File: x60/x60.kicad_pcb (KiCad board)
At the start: 2 copper layers, 0.1 x 0.5 mm, 150 parts, among them SW1 SW_Push, U1 ATmega32U4-AU, Y1 16mhz

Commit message: rearranged lines after stabs flip
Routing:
- net COL3: track 242.7 -> 248.7 mm
- net COL5: track 176.8 -> 177.8 mm
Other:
- board size 0.1 x 0.5 mm -> 285.7 x 95.2 mm
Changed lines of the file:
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@@
   (general
     (thickness 1.6)
-    (drawings 4)
-    (tracks 1052)
+    (drawings 5)
+    (tracks 1055)
     (zones 0)
     (modules 150)
@@
     )
   )
-  (gr_line (start 69.265 112.985) (end 69.325 112.715) (layer Edge.Cuts) (width 0.05))
-  (gr_line (start 69.245 113.035) (end 69.265 112.985) (layer Edge.Cuts) (width 0.05))
-  (gr_line (start 69.235 113.205) (end 69.245 113.035) (layer Edge.Cuts) (width 0.05))
+  (gr_line (start 69.325 204.405) (end 355.025 204.425) (layer Edge.Cuts) (width 0.05))
+  (gr_line (start 69.325 109.205) (end 69.325 204.405) (layer Edge.Cuts) (width 0.05))
+  (gr_line (start 355.025 109.225) (end 69.325 109.205) (layer Edge.Cuts) (width 0.05))
+  (gr_line (start 355.025 204.425) (end 355.025 109.225) (layer Edge.Cuts) (width 0.05))
   (gr_text x60 (at 311.29375 276.78125) (layer F.Cu)
     (effects (font (size 1.5 1.5) (thickness 0.3)))
@@
   (segment (start 72.5325 121.64625) (end 88.17875 121.64625) (width 0.254) (layer B.Cu) (net 7))
   (segment (start 71.4275 122.75125) (end 72.5325 121.64625) (width 0.254) (layer B.Cu) (net 7))
-  (segment (start 71.4275 142.739183) (end 71.4275 122.75125) (width 0.254) (layer B.Cu) (net 7))
   (segment (start 71.34948 142.817203) (end 71.4275 142.739183) (width 0.254) (layer B.Cu) (net 7))
-  (segment (start 182.46875 199.49525) (end 178.46496 203.49904) (width 0.254) (layer B.Cu) (net 7))
-  (segment (start 182.46875 198.49125) (end 182.46875 199.49525) (width 0.254) (layer B.Cu) (net 7))
-  (segment (start 178.46496 203.49904) (end 167.93529 203.49904) (width 0.254) (layer B.Cu) (net 7))
-  (segment (start 167.93529 203.49904) (end 164.243577 199.807327) (width 0.254) (layer B.Cu) (net 7))
   (segment (start 71.34948 198.335297) (end 71.34948 142.817203) (width 0.254) (layer B.Cu) (net 7))
-  (segment (start 164.243577 199.807327) (end 72.82151 199.807327) (width 0.254) (layer B.Cu) (net 7))
+  (segment (start 182.46875 198.49125) (end 182.46875 199.49525) (width 0.254) (layer B.Cu) (net 7))
+  (segment (start 178.46496 203.49904) (end 167.941156 203.49904) (width 0.254) (layer B.Cu) (net 7))
+  (segment (start 182.46875 199.49525) (end 178.46496 203.49904) (width 0.254) (layer B.Cu) (net 7))
+  (segment (start 167.941156 203.49904) (end 167.675203 203.233086) (width 0.254) (layer B.Cu) (net 7))
+  (segment (start 167.675203 203.233086) (end 164.249444 199.807327) (width 0.254) (layer B.Cu) (net 7))
+  (segment (start 71.4275 142.739183) (end 71.4275 122.75125) (width 0.254) (layer B.Cu) (net 7))
   (segment (start 72.82151 199.807327) (end 71.34948 198.335297) (width 0.254) (layer B.Cu) (net 7))
+  (segment (start 164.249444 199.807327) (end 72.82151 199.807327) (width 0.254) (layer B.Cu) (net 7))
   (segment (start 86.10625 132.67875) (end 94.7425 132.67875) (width 0.254) (layer B.Cu) (net 8))
   (segment (start 94.7425 132.67875) (end 95.61625 133.5525) (width 0.254) (layer B.Cu) (net 8))
@@
   (segment (start 186.376392 202.93076) (end 184.052191 200.606559) (width 0.254) (layer B.Cu) (net 15))
   (segment (start 139.12875 197.19625) (end 139.1625 197.19625) (width 0.254) (layer B.Cu) (net 15))
-  (segment (start 139.1625 197.19625) (end 139.7875 197.82125) (width 0.254) (layer B.Cu) (net 15))
   (via (at 164.563963 197.57326) (size 0.8) (drill 0.4) (layers F.Cu B.Cu) (net 15))
-  (segment (start 139.7875 197.82125) (end 140.03549 197.57326) (width 0.254) (layer B.Cu) (net 15))
   (segment (start 140.03549 197.57326) (end 164.563963 197.57326) (width 0.254) (layer B.Cu) (net 15))
   (segment (start 168.57625 200.59) (end 184.06875 200.59) (width 0.254) (layer F.Cu) (net 15))
@@
   (segment (start 164.563963 197.57326) (end 165.55951 197.57326) (width 0.254) (layer F.Cu) (net 15))
   (via (at 184.06875 200.59) (size 0.8) (drill 0.4) (layers F.Cu B.Cu) (net 15))
+  (segment (start 139.12875 197.19625) (end 139.20625 197.19625) (width 0.254) (layer B.Cu) (net 15))
+  (segment (start 139.58326 197.57326) (end 140.03549 197.57326) (width 0.254) (layer B.Cu) (net 15))
+  (segment (start 139.20625 197.19625) (end 139.58326 197.57326) (width 0.254) (layer B.Cu) (net 15))
   (segment (start 100.39375 113.62875) (end 104.68 113.62875) (width 0.254) (layer B.Cu) (net 16))
   (segment (start 104.68 113.62875) (end 105.79125 114.74) (width 0.254) (layer B.Cu) (net 16))
@@
   (segment (start 130.509375 184.320625) (end 128.09625 186.73375) (width 0.254) (layer F.Cu) (net 75))
   (segment (start 101.1875 192.36875) (end 103.56875 192.36875) (width 0.254) (layer B.Cu) (net 75))
-  (segment (start 178.81095 203.95305) (end 167.6793 203.95305) (width 0.254) (layer B.Cu) (net 75))
-  (segment (start 183.26875 198.49125) (end 183.26875 199.49525) (width 0.254) (layer B.Cu) (net 75))
-  (segment (start 183.26875 199.49525) (end 178.81095 203.95305) (width 0.254) (layer B.Cu) (net 75))
-  (segment (start 167.6793 203.95305) (end 166.1575 202.43125) (width 0.254) (layer B.Cu) (net 75))
-  (via (at 101.2375 200.534327) (size 0.8) (drill 0.4) (layers F.Cu B.Cu) (net 75))
-  (segment (start 166.1575 202.43125) (end 164.260577 200.534327) (width 0.254) (layer B.Cu) (net 75))
-  (segment (start 164.260577 200.534327) (end 101.2375 200.534327) (width 0.254) (layer B.Cu) (net 75))
-  (segment (start 99.59651 192.36875) (end 101.1875 192.36875) (width 0.254) (layer F.Cu) (net 75))
-  (segment (start 98.715499 193.249761) (end 99.59651 192.36875) (width 0.254) (layer F.Cu) (net 75))
-  (segment (start 98.715499 197.446641) (end 98.715499 193.249761) (width 0.254) (layer F.Cu) (net 75))
-  (segment (start 101.2375 199.968642) (end 98.715499 197.446641) (width 0.254) (layer F.Cu) (net 75))
-  (segment (start 101.2375 200.534327) (end 101.2375 199.968642) (width 0.254) (layer F.Cu) (net 75))
+  (segment (start 99.59651 192.36875) (end 99.59026 192.375) (width 0.254) (layer F.Cu) (net 75))
+  (segment (start 101.1875 192.36875) (end 99.59651 192.36875) (width 0.254) (layer F.Cu) (net 75))
+  (segment (start 99.59026 192.375) (end 97.875 192.375) (width 0.254) (layer F.Cu) (net 75))
+  (segment (start 97.875 192.375) (end 97.025 193.225) (width 0.254) (layer F.Cu) (net 75))
+  (segment (start 97.025 193.225) (end 97.025 202.485) (width 0.254) (layer F.Cu) (net 75))
+  (via (at 99.645006 203.782122) (size 0.8) (drill 0.4) (layers F.Cu B.Cu) (net 75))
+  (segment (start 97.025 202.485) (end 98.322122 203.782122) (width 0.254) (layer F.Cu) (net 75))
+  (segment (start 98.322122 203.782122) (end 99.645006 203.782122) (width 0.254) (layer F.Cu) (net 75))
+  (segment (start 183.26875 199.49525) (end 183.26875 198.49125) (width 0.254) (layer B.Cu) (net 75))
+  (segment (start 178.81095 203.95305) (end 183.26875 199.49525) (width 0.254) (layer B.Cu) (net 75))
+  (segment (start 100.381619 203.95305) (end 178.81095 203.95305) (width 0.254) (layer B.Cu) (net 75))
+  (segment (start 100.210691 203.782122) (end 100.381619 203.95305) (width 0.254) (layer B.Cu) (net 75))
+  (segment (start 99.645006 203.782122) (end 100.210691 203.782122) (width 0.254) (layer B.Cu) (net 75))
   (segment (start 134.58875 135.21875) (end 141.66875 135.21875) (width 0.254) (layer F.Cu) (net 76))
   (segment (start 133.71625 134.34625) (end 134.58875 135.21875) (width 0.254) (layer F.Cu) (net 76))
@@
   (segment (start 169.45 167.7625) (end 175.00625 173.31875) (width 0.254) (layer F.Cu) (net 100))
   (segment (start 162.37 167.7625) (end 169.45 167.7625) (width 0.254) (layer F.Cu) (net 100))
-  (segment (start 169.45 167.7625) (end 169.45 179.575) (width 0.254) (layer F.Cu) (net 100))
-  (segment (start 169.45 179.575) (end 163.085 185.94) (width 0.254) (layer F.Cu) (net 100))
-  (segment (start 163.085 185.94) (end 132.9225 185.94) (width 0.254) (layer F.Cu) (net 100))
-  (segment (start 128.506249 191.243751) (end 127.38125 192.36875) (width 0.254) (layer F.Cu) (net 100))
-  (segment (start 128.506249 190.356251) (end 128.506249 191.243751) (width 0.254) (layer F.Cu) (net 100))
-  (segment (start 132.9225 185.94) (end 128.506249 190.356251) (width 0.254) (layer F.Cu) (net 100))
   (segment (start 127.38125 192.36875) (end 125 192.36875) (width 0.254) (layer F.Cu) (net 100))
   (via (at 189.501468 180.807282) (size 0.8) (drill 0.4) (layers F.Cu B.Cu) (net 100))
@@
   (segment (start 188.33 173.31875) (end 175.00625 173.31875) (width 0.254) (layer F.Cu) (net 100))
   (segment (start 188.3775 173.27125) (end 188.33 173.31875) (width 0.254) (layer F.Cu) (net 100))
+  (segment (start 169.45 179.575) (end 169.45 167.7625) (width 0.254) (layer F.Cu) (net 100))
+  (segment (start 165.05 183.975) (end 169.45 179.575) (width 0.254) (layer F.Cu) (net 100))
+  (segment (start 133.265 183.975) (end 165.05 183.975) (width 0.254) (layer F.Cu) (net 100))
+  (segment (start 128.506249 188.733751) (end 133.265 183.975) (width 0.254) (layer F.Cu) (net 100))
+  (segment (start 127.38125 192.36875) (end 128.506249 191.243751) (width 0.254) (layer F.Cu) (net 100))
+  (segment (start 128.506249 191.243751) (end 128.506249 188.733751) (width 0.254) (layer F.Cu) (net 100))
 )

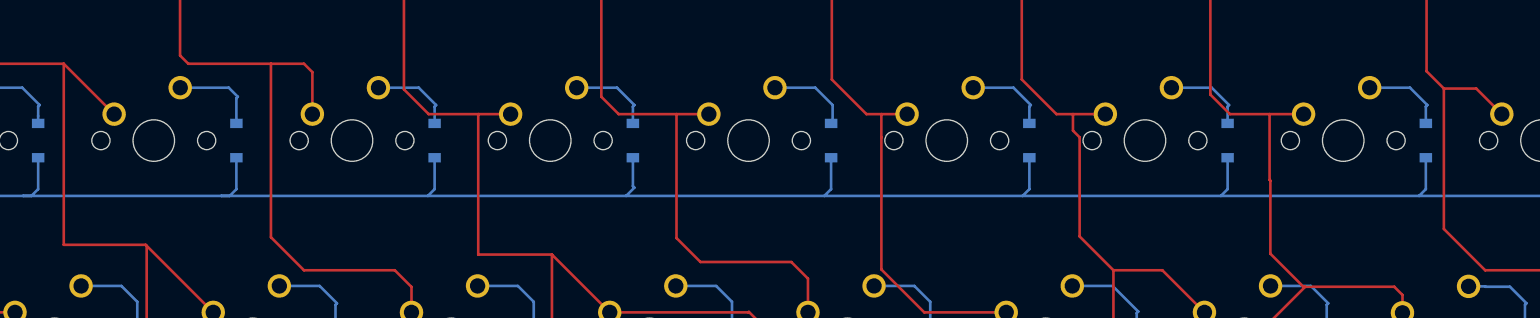
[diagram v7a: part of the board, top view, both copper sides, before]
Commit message: adjusted some routing
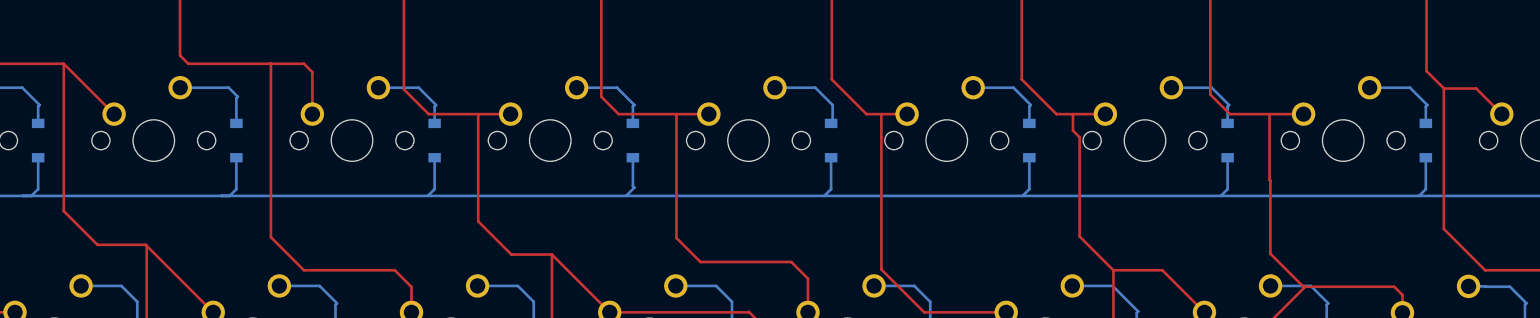
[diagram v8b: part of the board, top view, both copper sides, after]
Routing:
- net COL3: track 248.7 -> 246.8 mm
- net COL5: track 177.8 -> 175.9 mm
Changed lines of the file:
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@@
     (thickness 1.6)
     (drawings 5)
-    (tracks 1055)
+    (tracks 1058)
     (zones 0)
     (modules 150)
@@
   (segment (start 122.54 149.4275) (end 127.38125 154.26875) (width 0.254) (layer F.Cu) (net 75))
   (segment (start 114.66625 149.4275) (end 122.54 149.4275) (width 0.254) (layer F.Cu) (net 75))
-  (segment (start 122.54 149.4275) (end 122.54 166.82625) (width 0.254) (layer F.Cu) (net 75))
-  (segment (start 122.54 166.82625) (end 130.41375 166.82625) (width 0.254) (layer F.Cu) (net 75))
   (segment (start 130.509375 166.921875) (end 136.90625 173.31875) (width 0.254) (layer F.Cu) (net 75))
-  (segment (start 130.41375 166.82625) (end 130.509375 166.921875) (width 0.254) (layer F.Cu) (net 75))
   (segment (start 103.56875 187.5425) (end 103.56875 192.36875) (width 0.254) (layer F.Cu) (net 75))
   (segment (start 103.55375 187.5275) (end 103.56875 187.5425) (width 0.254) (layer F.Cu) (net 75))
@@
   (segment (start 100.210691 203.782122) (end 100.381619 203.95305) (width 0.254) (layer B.Cu) (net 75))
   (segment (start 99.645006 203.782122) (end 100.210691 203.782122) (width 0.254) (layer B.Cu) (net 75))
+  (segment (start 130.41375 166.82625) (end 130.509375 166.921875) (width 0.254) (layer F.Cu) (net 75))
+  (segment (start 125.78375 166.82625) (end 130.41375 166.82625) (width 0.254) (layer F.Cu) (net 75))
+  (segment (start 122.54 163.5825) (end 125.78375 166.82625) (width 0.254) (layer F.Cu) (net 75))
+  (segment (start 122.54 149.4275) (end 122.54 163.5825) (width 0.254) (layer F.Cu) (net 75))
   (segment (start 134.58875 135.21875) (end 141.66875 135.21875) (width 0.254) (layer F.Cu) (net 76))
   (segment (start 133.71625 134.34625) (end 134.58875 135.21875) (width 0.254) (layer F.Cu) (net 76))
@@
   (segment (start 253.49375 135.21875) (end 255.96875 135.21875) (width 0.254) (layer F.Cu) (net 81))
   (segment (start 251.27 135.21875) (end 253.49375 135.21875) (width 0.254) (layer F.Cu) (net 81))
-  (segment (start 253.496749 150.145499) (end 255.16 151.80875) (width 0.254) (layer F.Cu) (net 81))
   (segment (start 258.27125 151.80875) (end 260.73125 154.26875) (width 0.254) (layer F.Cu) (net 81))
-  (segment (start 255.16 151.80875) (end 258.27125 151.80875) (width 0.254) (layer F.Cu) (net 81))
   (segment (start 270.25625 170.08) (end 270.25625 173.31875) (width 0.254) (layer F.Cu) (net 81))
   (segment (start 269.4475 169.27125) (end 270.25625 170.08) (width 0.254) (layer F.Cu) (net 81))
@@
   (segment (start 196.0475 198.19125) (end 238.3475 198.19125) (width 0.254) (layer F.Cu) (net 81))
   (segment (start 238.3475 198.19125) (end 239.0275 197.51125) (width 0.254) (layer F.Cu) (net 81))
+  (segment (start 253.496749 150.145499) (end 253.505499 150.145499) (width 0.254) (layer F.Cu) (net 81))
+  (segment (start 255.16875 151.80875) (end 258.27125 151.80875) (width 0.254) (layer F.Cu) (net 81))
+  (segment (start 253.505499 150.145499) (end 255.16875 151.80875) (width 0.254) (layer F.Cu) (net 81))
   (via (at 191.0075 194.401253) (size 0.8) (drill 0.4) (layers F.Cu B.Cu) (net 82))
   (segment (start 189.340686 194.401253) (end 191.0075 194.401253) (width 0.254) (layer B.Cu) (net 82))
@@
   (segment (start 155.22625 135.21875) (end 155.22625 151.8875) (width 0.254) (layer F.Cu) (net 100))
   (segment (start 155.22625 151.8875) (end 157.6075 154.26875) (width 0.254) (layer F.Cu) (net 100))
-  (segment (start 162.37 154.26875) (end 162.37 167.7625) (width 0.254) (layer F.Cu) (net 100))
   (segment (start 162.37 154.26875) (end 165.48125 154.26875) (width 0.254) (layer F.Cu) (net 100))
   (segment (start 157.6075 154.26875) (end 162.37 154.26875) (width 0.254) (layer F.Cu) (net 100))
   (segment (start 169.45 167.7625) (end 175.00625 173.31875) (width 0.254) (layer F.Cu) (net 100))
-  (segment (start 162.37 167.7625) (end 169.45 167.7625) (width 0.254) (layer F.Cu) (net 100))
   (segment (start 127.38125 192.36875) (end 125 192.36875) (width 0.254) (layer F.Cu) (net 100))
   (via (at 189.501468 180.807282) (size 0.8) (drill 0.4) (layers F.Cu B.Cu) (net 100))
@@
   (segment (start 127.38125 192.36875) (end 128.506249 191.243751) (width 0.254) (layer F.Cu) (net 100))
   (segment (start 128.506249 191.243751) (end 128.506249 188.733751) (width 0.254) (layer F.Cu) (net 100))
+  (segment (start 165.5575 167.7625) (end 169.45 167.7625) (width 0.254) (layer F.Cu) (net 100))
+  (segment (start 162.37 164.575) (end 165.5575 167.7625) (width 0.254) (layer F.Cu) (net 100))
+  (segment (start 162.37 154.26875) (end 162.37 164.575) (width 0.254) (layer F.Cu) (net 100))
 )
